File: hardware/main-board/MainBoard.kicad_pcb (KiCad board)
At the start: 4 copper layers, 120 x 135 mm, 145 parts, among them J1 Conn_01x03_Pin, J10 USB_C_Receptacle_USB2.0_14P, J11 Conn_02x05_Odd_Even, J12 Conn_01x02_Pin, J13 Conn_01x02_Pin, J2 Conn_01x03_Pin, J3 Conn_01x03_Pin, J4 Conn_01x03_Pin, J5 Conn_01x02_Pin, J6 Conn_01x02_Pin, J7 Conn_01x02_Pin, J8 Conn_01x02_Pin, J9 Barrel_Jack, SW1 SW_SP3T, SW2 SW_SP3T, SW3 SW_SPST, SW4 SW_SPST, U1 CD22M3494MQZ, U10 TL071, U11 CD22M3494MQZ, U12 CD22M3494MQZ, U13 TL071, U14 AD5263BRUZ200, U15 AD5263BRUZ200, U16 TL071, U17 CD22M3494MQZ, U18 CD22M3494MQZ, U19 TL071, U2 TL081, U20 AD5263BRUZ200, U21 AD5263BRUZ200, U22 TL071, U23 CD22M3494MQZ, U24 CD22M3494MQZ, U25 TL071, U26 AD5263BRUZ200, U27 AD5263BRUZ200, U28 TL071, U29 CD22M3494MQZ, U3 TL071, U30 CD22M3494MQZ, U31 XTPS55285VALR, U32 TPS54202DDC, U33 LM2776, U34 74HC164, U35 FT232RL, U36 74HC164, U37 STM32F091RCTx, U38 74HC164, U4 TL071, U5 TL071, U6 TL071, U7 TL071, U8 AD5263BRUZ200, U9 AD5263BRUZ200

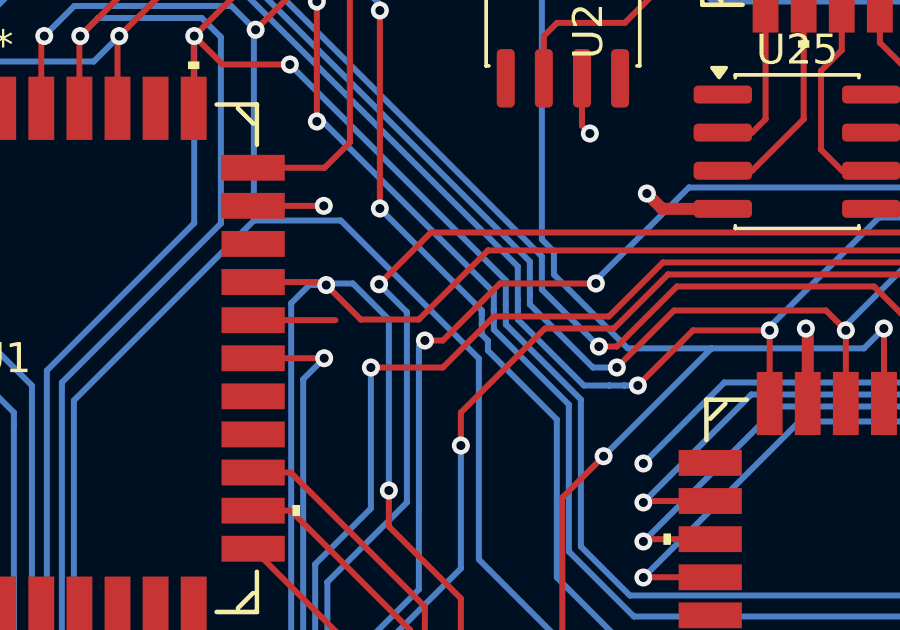
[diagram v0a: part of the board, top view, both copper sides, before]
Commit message: feat: Routing for top level +/- 5V
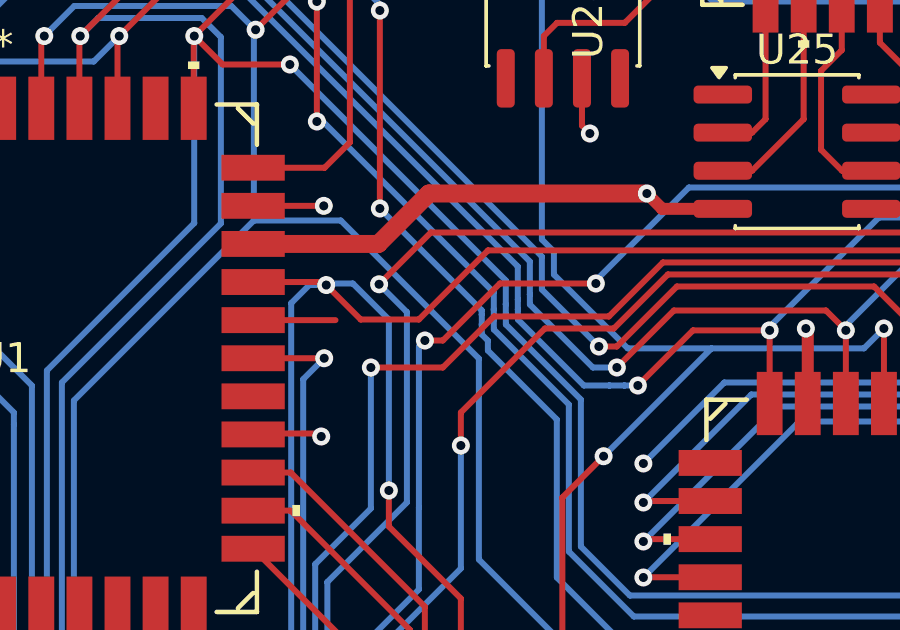
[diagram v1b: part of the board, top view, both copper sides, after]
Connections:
- U1 pad 32: unconnected-(U1A-Y0-Pad32) -> +5V
- U1 pad 37: unconnected-(U1A-Y2-Pad37) -> -5V
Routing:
- net -5V: track 671.1 -> 684.9 mm
- net +5V: track 151.7 -> 154.0 mm, vias 41 -> 42

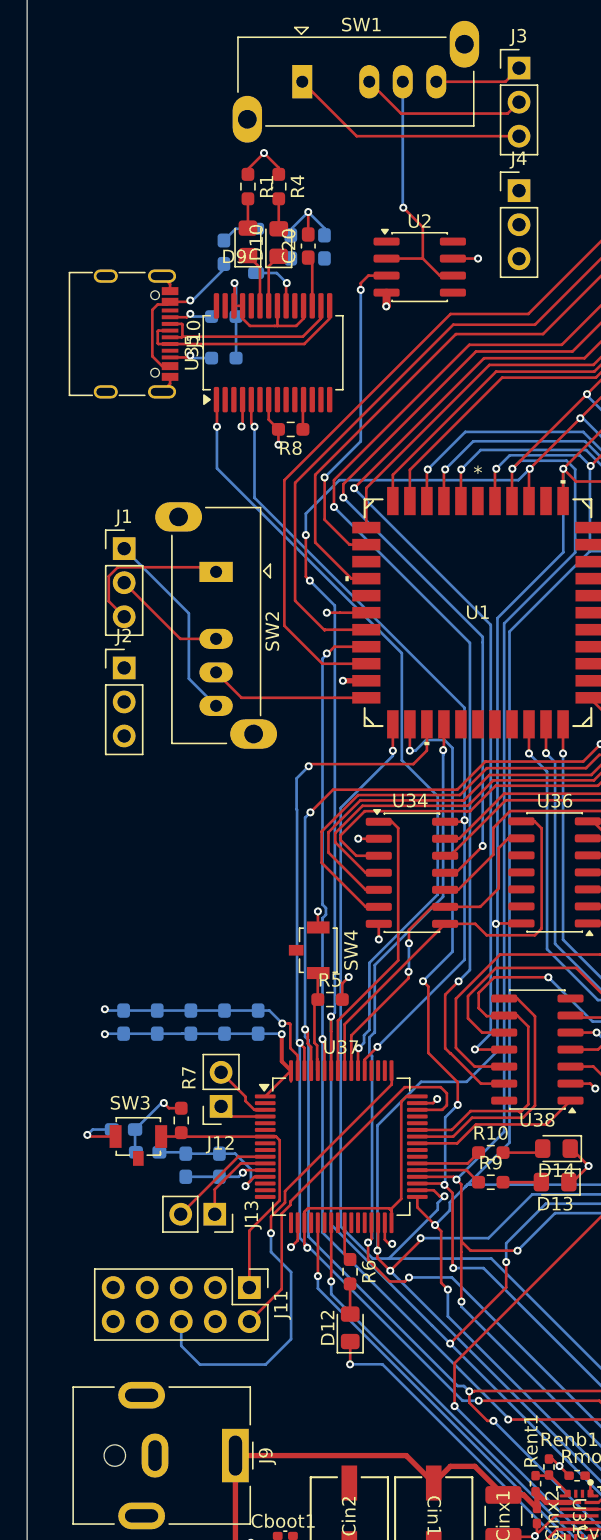
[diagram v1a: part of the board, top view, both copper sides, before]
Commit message: added ground conn and fixed switches
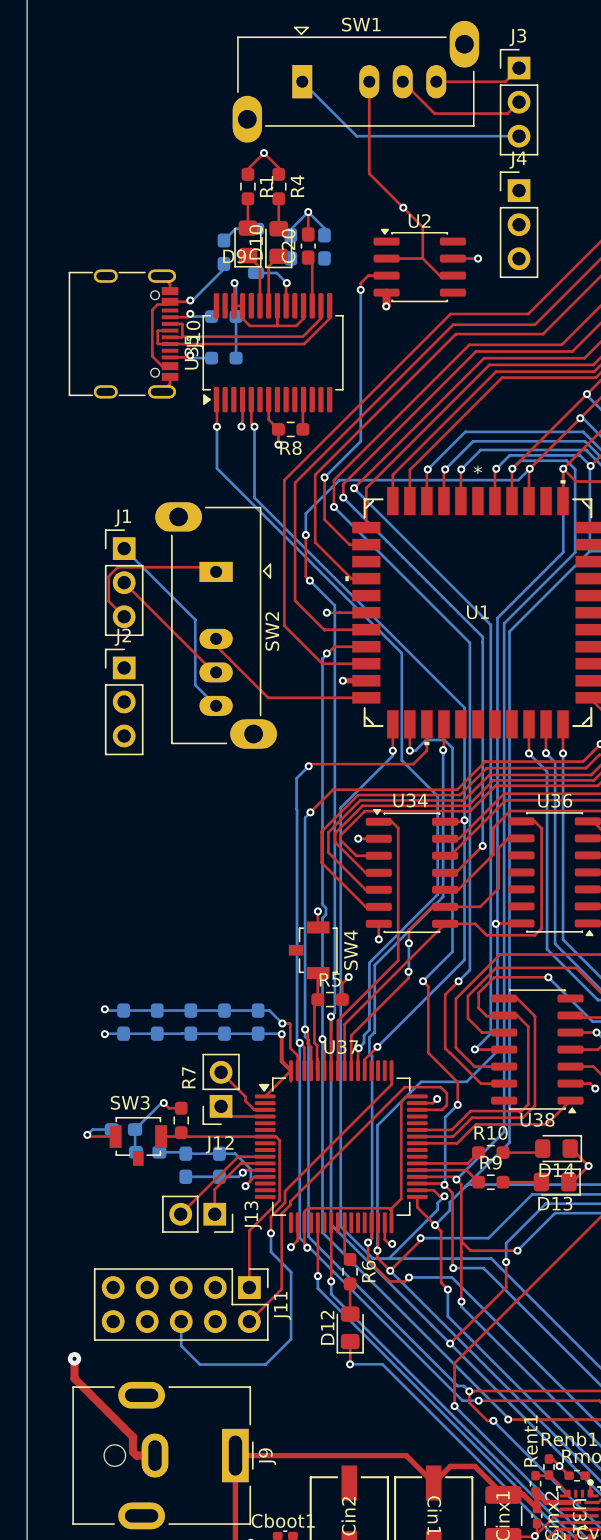
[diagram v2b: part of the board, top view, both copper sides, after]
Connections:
- C18 pad 1: GNDPWR -> GND
- C19 pad 1: GNDPWR -> GND
- Ccomp1 pad 2: GNDPWR -> GND
- Ccomp2 pad 2: GNDPWR -> GND
- Cin2 pad 2: GNDPWR -> GND
- Cin5 pad 1: GNDPWR -> GND
- Cinx1 pad 2: GNDPWR -> GND
- Cinx2 pad 2: GNDPWR -> GND
- Cinx3 pad 1: GNDPWR -> GND
- Cout2 pad 1: GNDPWR -> GND
- Cout3 pad 2: GNDPWR -> GND
- Coutx1 pad 2: GNDPWR -> GND
- Coutx2 pad 1: GNDPWR -> GND
- Coutx3 pad 2: GNDPWR -> GND
- Cvcc1 pad 2: GNDPWR -> GND
- J9 pad 2: GNDPWR -> GND
- Renb1 pad 2: GNDPWR -> GND
- Rfbb1 pad 2: GNDPWR -> GND
- Rfbb2 pad 2: GNDPWR -> GND
- Rmode1 pad 2: GNDPWR -> GND
- SW1 pad 2: Net-(J3-Pin_2) -> /Signal_Out
- SW1 pad 3: /Signal_Out -> Net-(J3-Pin_2)
- SW2 pad 2: Net-(J1-Pin_2) -> /Signal_In
- SW2 pad 3: /Signal_In -> Net-(J1-Pin_2)
- U31 pad 7: GNDPWR -> GND
- U32 pad 1: GNDPWR -> GND
- U33 pad 2: GNDPWR -> GND
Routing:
- net GND: track 153.0 -> 216.3 mm, vias 33 -> 42
- net GNDPWR: track 52.8 -> 0.00 mm, vias 8 -> 0
- net Net-(J3-Pin_2): track 12.5 -> 10.0 mm
- net /Signal_In: track 12.0 -> 13.3 mm
- net /Signal_Out: track 19.6 -> 20.7 mm
- net Net-(J1-Pin_2): track 8.60 -> 9.63 mm
- removed copper zone on In1.Cu, net GNDPWR

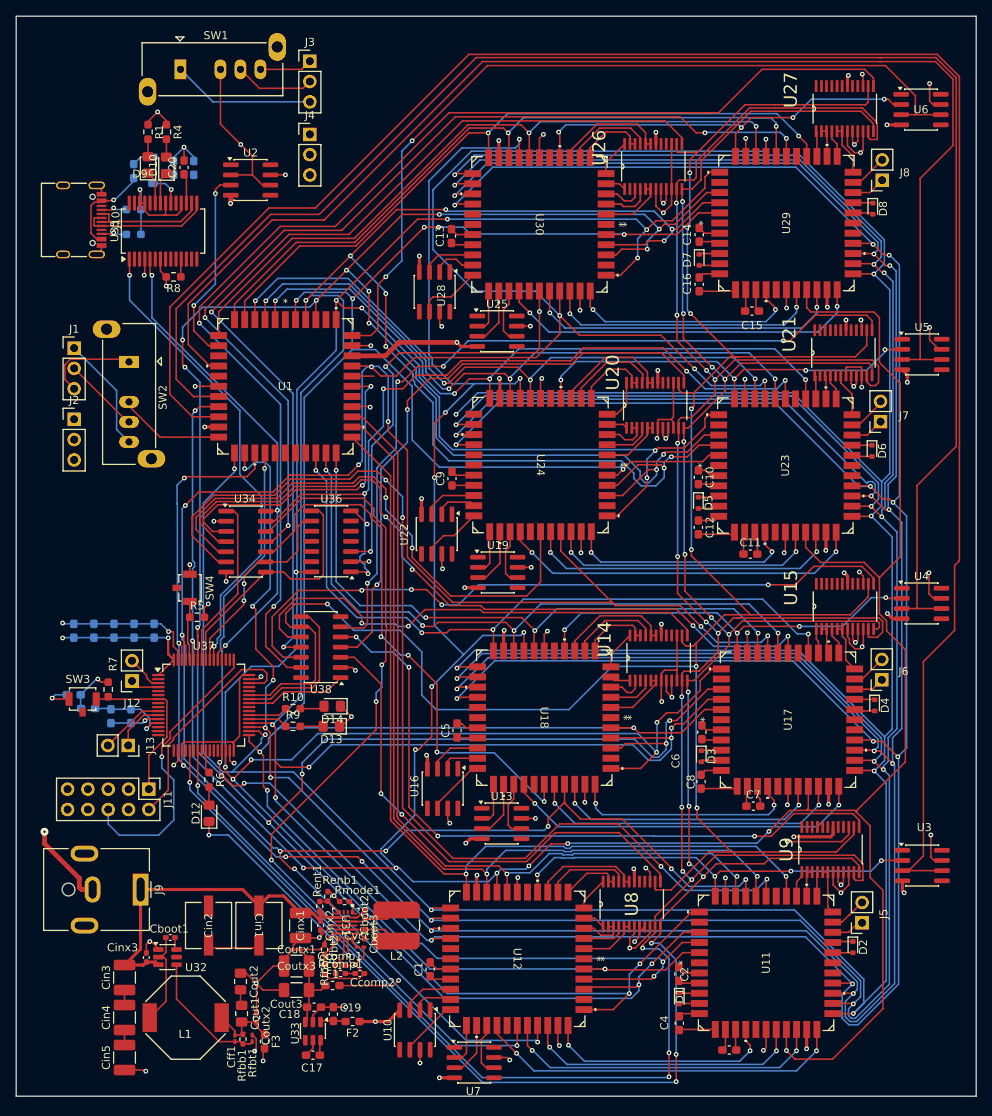
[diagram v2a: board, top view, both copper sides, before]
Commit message: feat: ERC + DRC fixes
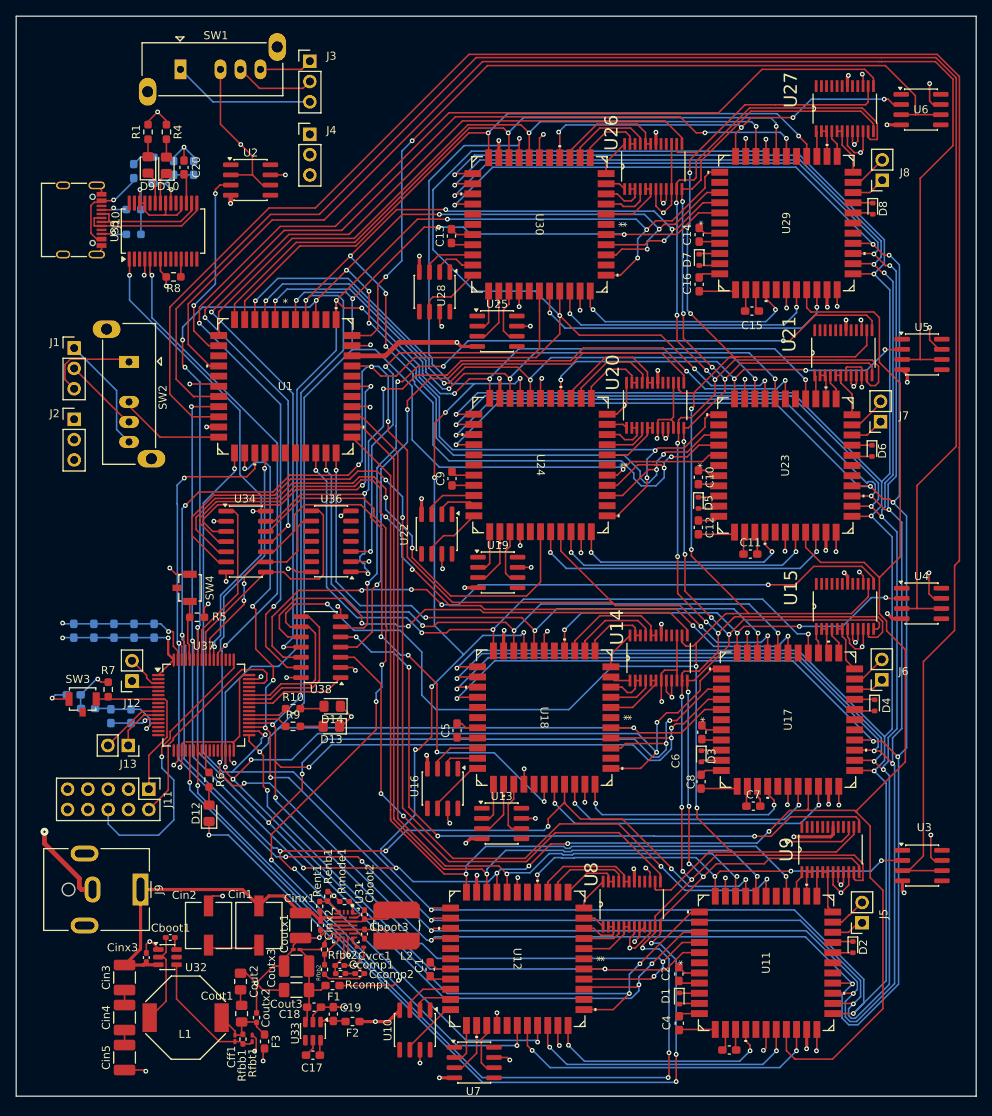
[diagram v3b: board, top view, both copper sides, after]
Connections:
- U11 pad 17: /STD/Y4 -> GND
- U12 pad 32: /STD/Y4 -> GND
- U17 pad 17: /STD1/Y4 -> GND
- U18 pad 32: /STD1/Y4 -> GND
- U23 pad 17: /STD2/Y4 -> GND
- U24 pad 32: /STD2/Y4 -> GND
- U29 pad 17: /STD3/Y4 -> GND
- U30 pad 32: /STD3/Y4 -> GND
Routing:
- net /STD/Y4: track 46.6 -> 0.00 mm, vias 2 -> 0
- net /STD3/Y4: track 46.6 -> 0.00 mm, vias 2 -> 0
- net /STD2/Y4: track 45.9 -> 0.00 mm, vias 2 -> 0
- net /STD1/Y4: track 45.6 -> 0.00 mm, vias 2 -> 0
- net GND: track 216.3 -> 236.6 mm, vias 42 -> 52
- net Net-(D11-K): track 4.32 -> 8.35 mm
- net +5V: track 154.0 -> 157.0 mm, vias 42 -> 43
- net unconnected-(U1A-Y1-Pad35): track 2.75 -> 0.00 mm
- net /MicroController/MT_AX1: track 444.8 -> 447.0 mm
- net +3.3V: track 55.1 -> 57.0 mm
- net -5V: track 684.9 -> 683.9 mm
- net /MicroController/MT_STB: track 418.6 -> 419.3 mm, vias 16 -> 15
- net /STD3/R1_out: track 5.19 -> 5.83 mm
- net /STD2/R6_out: track 5.50 -> 6.14 mm
- net /STD2/R5_out: track 2.99 -> 3.62 mm
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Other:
- board text removed: "${REFERENCE}"

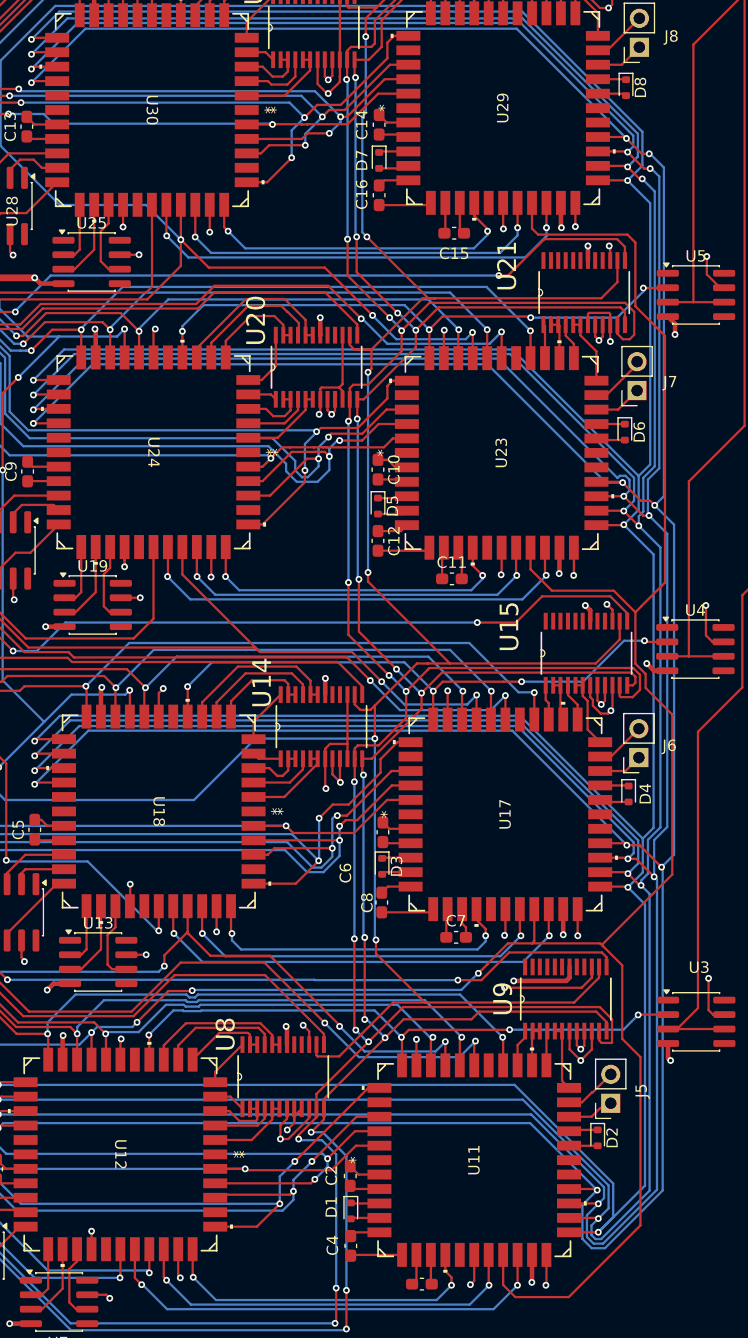
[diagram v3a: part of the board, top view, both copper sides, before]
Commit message: feat: Diodes bigger
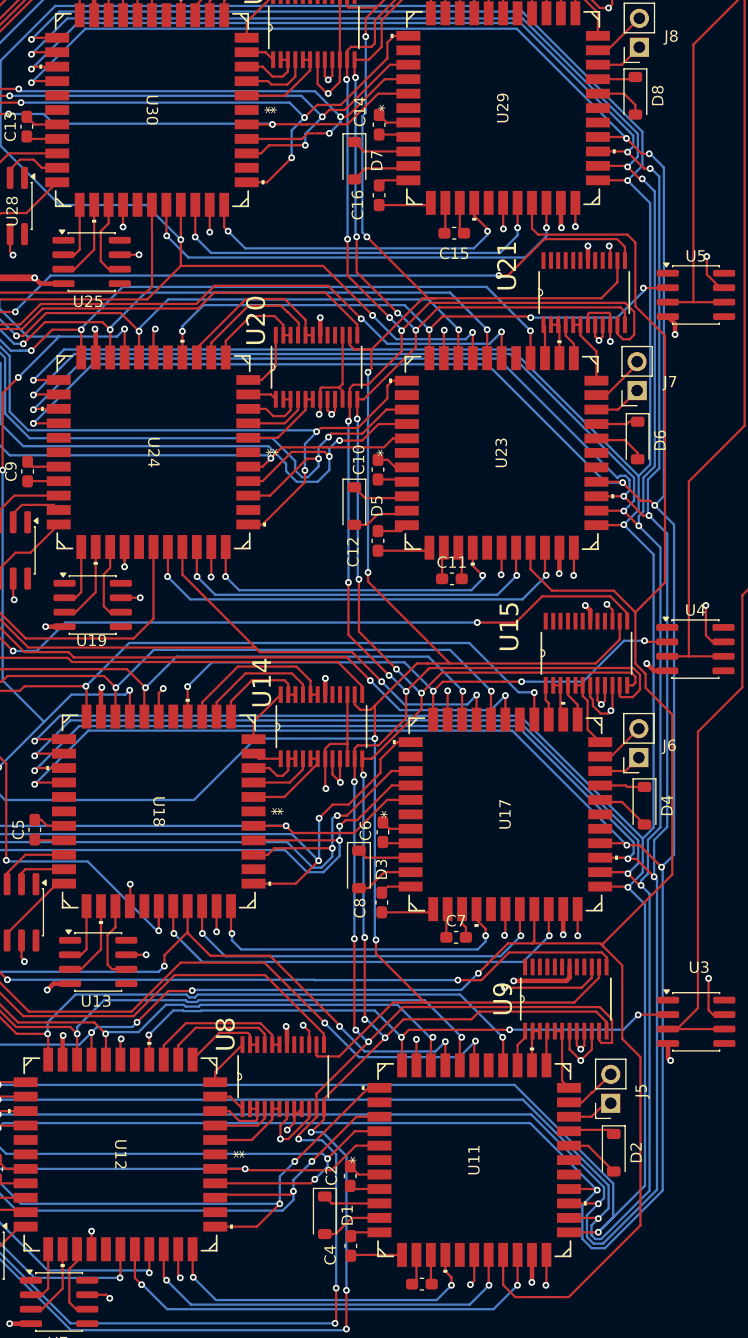
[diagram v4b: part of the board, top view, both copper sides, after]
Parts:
- D1, D2, D3, D4, D5, D6, D7, D8: footprint Diode_SMD:D_SOD-523 -> Diode_SMD:D_SOD-123
- moved D1 2.32 mm to (136.6, 152.6)
- moved D7 2.18 mm to (139.2, 59.9)
- moved D5 2.07 mm to (139.2, 90.3)
- moved D3 2.06 mm to (139.6, 122.2)
- moved D2 1.92 mm to (162.0, 147.1)
- moved D4 1.73 mm to (164.7, 116.6)
- moved D6 1.35 mm to (164.1, 84.5)
- moved D8 1.09 mm to (163.9, 54.2)
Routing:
- net /STD/D1_anode: track 2.55 -> 5.39 mm
- net /STD3/D1_anode: track 2.66 -> 5.24 mm
- net /STD/D1_cathode: track 2.54 -> 5.06 mm
- net /STD3/D1_cathode: track 2.61 -> 5.09 mm
- net /STD2/D1_cathode: track 2.61 -> 5.07 mm
- net /STD2/D1_anode: track 2.66 -> 5.13 mm
- net /STD1/D2_anode: track 2.37 -> 4.79 mm
- net /STD/D2_anode: track 2.52 -> 4.87 mm
- net /STD1/D1_anode: track 2.91 -> 5.13 mm
- net /STD2/D2_anode: track 2.56 -> 4.71 mm
- net /STD1/D1_cathode: track 2.67 -> 4.80 mm
- net /STD3/D2_anode: track 2.54 -> 4.55 mm
- net /STD1/D2_cathode: track 2.32 -> 3.95 mm
- net /STD/D2_cathode: track 2.57 -> 4.13 mm
- net /STD2/D2_cathode: track 2.50 -> 3.72 mm
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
